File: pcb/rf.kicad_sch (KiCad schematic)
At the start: 0 parts

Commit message: tons of work on rf and mcu
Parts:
- added C41, C51: 22uF, symbol Device:C_Small
- added C42: 4.7uF, symbol Device:C_Small
- added C43, C44: 100nF, symbol Device:C_Small
- added C45: 1uF, symbol Device:C_Small
- added C46, C47: 1uF, symbol Device:C
- added C48, C49: 2.2uF, symbol Device:C
- added C50: 1nF, symbol Device:C
- added C52, C53, C54, C55, C56, C57, C58, C59, C60, C61, C62, C63, C64, C65, C66, C67: C, symbol Device:C
- added D2, D3: D_TVS, symbol Device:D_TVS
- added FB3, FB4, FB5: FerriteBead_Small, symbol Device:FerriteBead_Small
- added J4, J5: Conn_Coaxial, symbol Connector:Conn_Coaxial
- added L10, L11, L12, L13, L14, L3, L4, L5, L6, L7, L8, L9: L, symbol Device:L
- added L2: 2.2uH, symbol Device:L
- added TP1: GPS_D-, symbol Connector:TestPoint
- added TP2: GPS_D+, symbol Connector:TestPoint
- added U4: ~, symbol lr2021_new:lr2021
- added U5: NEO-M9N, RF_GPS:ublox_NEO, symbol RF_GPS:NEO-M9N
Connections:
- new net: C58.1, C59.1, L8.2
- new net: C57.1, C59.2, D2.2 (A2), J4.1 (In), L6.2, L7.1
- new net: C61.1, C62.1, L10.2
- new net: C53.1, L4.2
- new net: C53.2, C54.1, C55.1, L5.1
- new net: FB5.2, U4.13 (VPAX1)
- new net: C63.1, L11.2
- new net: C65.2, C66.1, L12.2, L13.1
- new net: C62.2, C67.1, D3.2 (A2), J5.1 (In), L13.2, L14.1
- new net: C55.2, C56.1, L5.2, L6.1
- new net: FB4.2, U4.12 (VDCC1)
- new net: L2.2, U4.14 (LXB)
- new net: L2.1, U4.16 (LXA)
- new net: U5.10 (GND), U5.12 (GND), U5.13 (GND), U5.24 (GND)
- new net: TP1.1, U5.5 (USB_DM)
- new net: TP2.1, U5.6 (USB_DP)
- new net: C63.2, C64.1, C65.1, L12.1
- new net +3.3V: FB3.1
- new net GND: C41.2, C42.2, C43.2, C44.2, C45.2, C46.2, C47.2, C48.2, C49.2, C50.2, C51.2, C52.1, C54.2, C56.2, C57.2, C58.2, C60.1, C61.2, C64.2, C66.2, C67.2, D2.1 (A1), D3.1 (A1), J4.2 (Ext), J5.2 (Ext), L14.2, L7.2, U4.0 (GND), U4.15 (GND_DCC), U4.30 (GND)
- new net hfi: L10.1, U4.31 (RFI_HF)
- new net hfo: L11.1, L9.2, U4.32 (RFO_HF)
- new net lfi: L8.1, U4.29 (RFI_LF)
- new net lfo: L3.2, L4.1, U4.27 (RFO_LF2), U4.28 (RFO_LF1)
- new net lr2021_vbat: C41.1, C42.1, C43.1, C44.1, C45.1, C51.1, FB3.2, U4.17 (VBAT)
- new net lr2021_vdcc: C46.1, C47.1, FB4.1, U4.26 (VDCC2)
- new net lr2021_vpax: C48.1, C49.1, FB5.1, U4.2 (VPAX2)
- new net lr_busy: U4.25 (BUSY)
- new net lr_irq1: U4.7 (DIO11)
- new net lr_irq2: U4.8 (DIO10)
- new net lr_miso: U4.21 (MISO)
- new net lr_mosi: U4.22 (MOSI)
- new net lr_nrst: U4.20 (NRST)
- new net lr_nss: U4.24 (NSS)
- new net lr_sck: U4.23 (SCK)
- new net vr_pa: C50.1, C52.2, C60.2, L3.1, L9.1, U4.1 (VR_PA)
- no-connect marks 0 -> 6
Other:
- note added: "semi insane vcc decoupling"
- note added: "vdcc decoupling"
- note added: "vpax decoupling"

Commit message: added missing files, rf stuff done I think (hope)
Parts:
- added AE1: Antenna, symbol Device:Antenna
- added C68: 100nF, symbol Device:C_Small
- added C69, C70: 22uF, symbol Device:C_Small
- added C71: 1uF, symbol Device:C
- added D4: D_TVS, symbol Device:D_TVS
- added JP1: NC, symbol Jumper:SolderJumper_2_Bridged
- added L15: 9.1nH, symbol Device:L
- added TP3: GPS_SDA, symbol Connector:TestPoint
- added TP4: GPS_SCL, symbol Connector:TestPoint
- added TP5: GPS_BOOT, symbol Connector:TestPoint
- added U6: ~, symbol alnd-wb-0013-t:ALND-WB-0013-T
- added Y3: ECS-TXO-32CSMV-320-AN-TR, ECSTXO32CSMV320ANTR, symbol ECS-TXO-32CSMV-320-AN-TR:ECS-TXO-32CSMV-320-AN-TR
- C52, C60: value C -> 47pF
- C53: value C -> 22pF
- C54: value C -> 7.5pF
- C55, C57: value C -> 1.8pF
- C56: value C -> 3.9pF
- C58: value C -> 2.2pF
- C59, C62: value C -> 18pF
- C61: value C -> idk; now not fitted
- C63: value C -> 6.8pF
- C64: value C -> 2.7pF
- C65: value C -> 1.1pF
- C66: value C -> 1.2pF
- C67: value C -> 2.0pF
- L10: value L -> 2.4nH
- L11: value L -> 1.5nH
- L12: value L -> 1.6nH
- L13: value L -> 1.1nH
- L14: value L -> idk; now not fitted
- L3: value L -> 12nH
- L4: value L -> 4.7nH
- L5: value L -> 3.9nH
- L6: value L -> 7.5nH
- L7: value L -> 22nH
- L8: value L -> 24nH
- L9: value L -> 18nH
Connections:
- net +3.3V: now also U5.22 (V_BCKP), U5.23 (VCC), U5.7 (VDD_USB), C69.1, C70.1, JP1.1 (A)
- net GND: now also U5.10 (GND), U5.12 (GND), U5.13 (GND), U5.24 (GND), C68.1, C69.2, C70.2, C71.2, D4.1 (A1), U6.1 (GND), U6.2 (GND), Y3.1 (GROUND_1), Y3.2 (GROUND_2)
- net lr_xtalin: now reaches U4.4 (XTA)
- net lr_xtalin: now also Y3.3 (OUTPUT)
- net lr_vtcxo: now reaches U4.6 (VTXCO)
- net lr_vtcxo: now also C68.2, Y3.4 (VDD)
- net at U5.1 (~{SAFEBOOT}): now also TP5.1
- net at U5.11 (RF_IN): now also U6.6 (RFOUT)
- net at U5.18 (SDA/~{SPI_CS}): now also TP3.1
- net at U5.19 (SCL/SPI_CLK): now also TP4.1
- net at U5.2 (D_SEL): now also JP1.2 (B)
- net gps_rx: now reaches U5.20 (TXD/SPI_MISO)
- net gps_tx: now reaches U5.21 (RXD/SPI_MOSI)
- net gps_pps: now reaches U5.3 (TIMEPULSE)
- net gps_rst: now reaches U5.8 (~{RESET})
- net at U5.9 (VCC_RF): now also C71.1, U6.4 (VDD), U6.5 (Ven)
- new net: AE1.1 (A), D4.2 (A2), L15.2
- new net: L15.1, U6.3 (RFIN)
- no-connect marks 6 -> 9
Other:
- note added: "32mhz tcxo"
- note added: "gps"
- note added: "high frequency matching"
- note added: "lora module"
- note added: "low frequency matching"
- moved on the sheet: C41, C42, C43, C44, C45, C46, C47, C48, C49, C50, C51, C52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

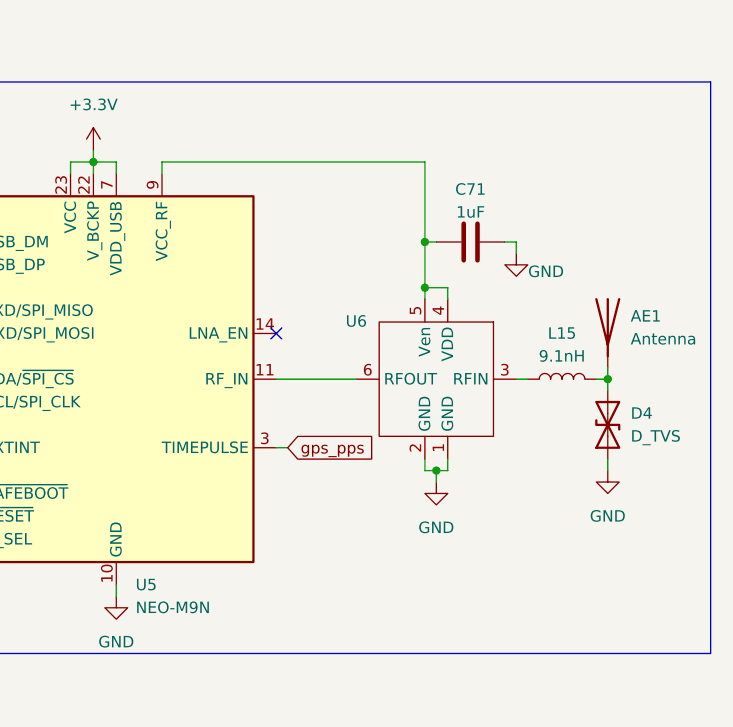
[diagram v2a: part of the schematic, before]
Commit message: sensors pretty much done (still need to add high g_
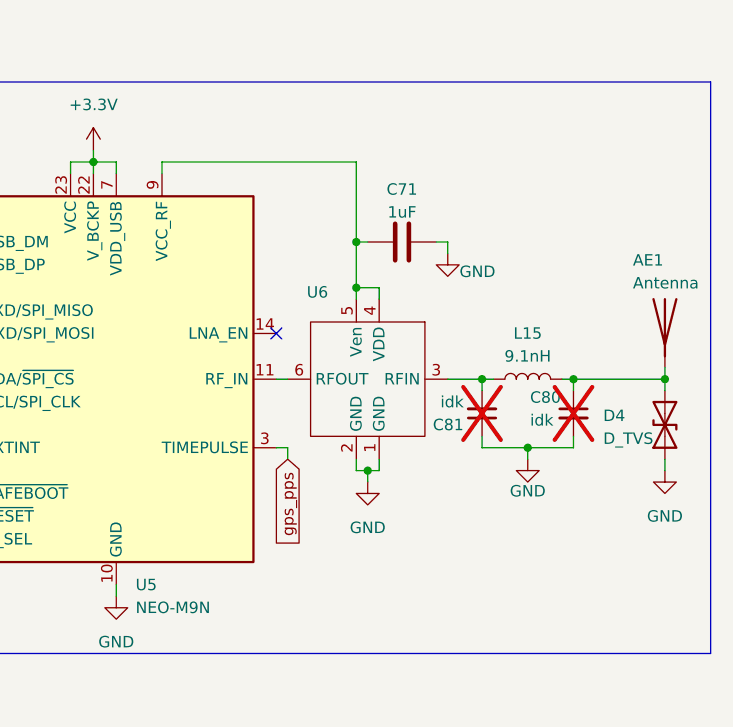
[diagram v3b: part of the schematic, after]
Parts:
- added C80, C81: idk, symbol Device:C_Small
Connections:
- net GND: now also C80.2, C81.1
- net at AE1.1 (A), D4.2 (A2), L15.2: now also C80.1
- net at L15.1, U6.3 (RFIN): now also C81.2
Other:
- moved on the sheet: AE1, C71, D4, L15, U6

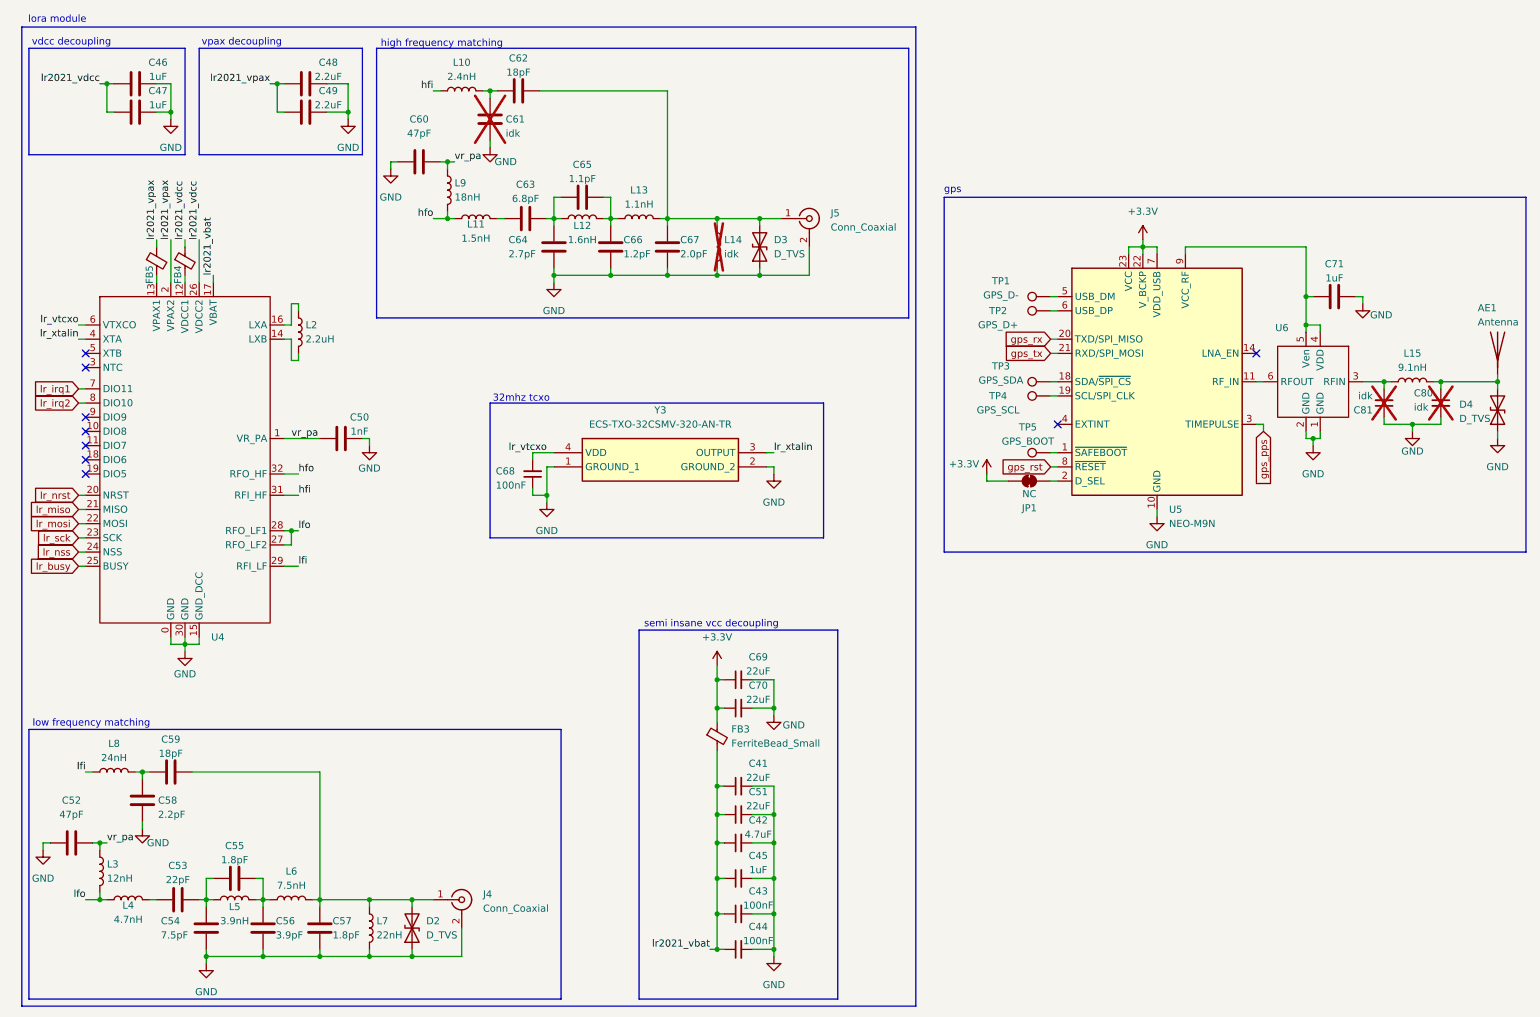
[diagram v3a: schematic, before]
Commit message: got fets figured out (finally), can integrated, a 5v regulator, sensors added - overall great progress!
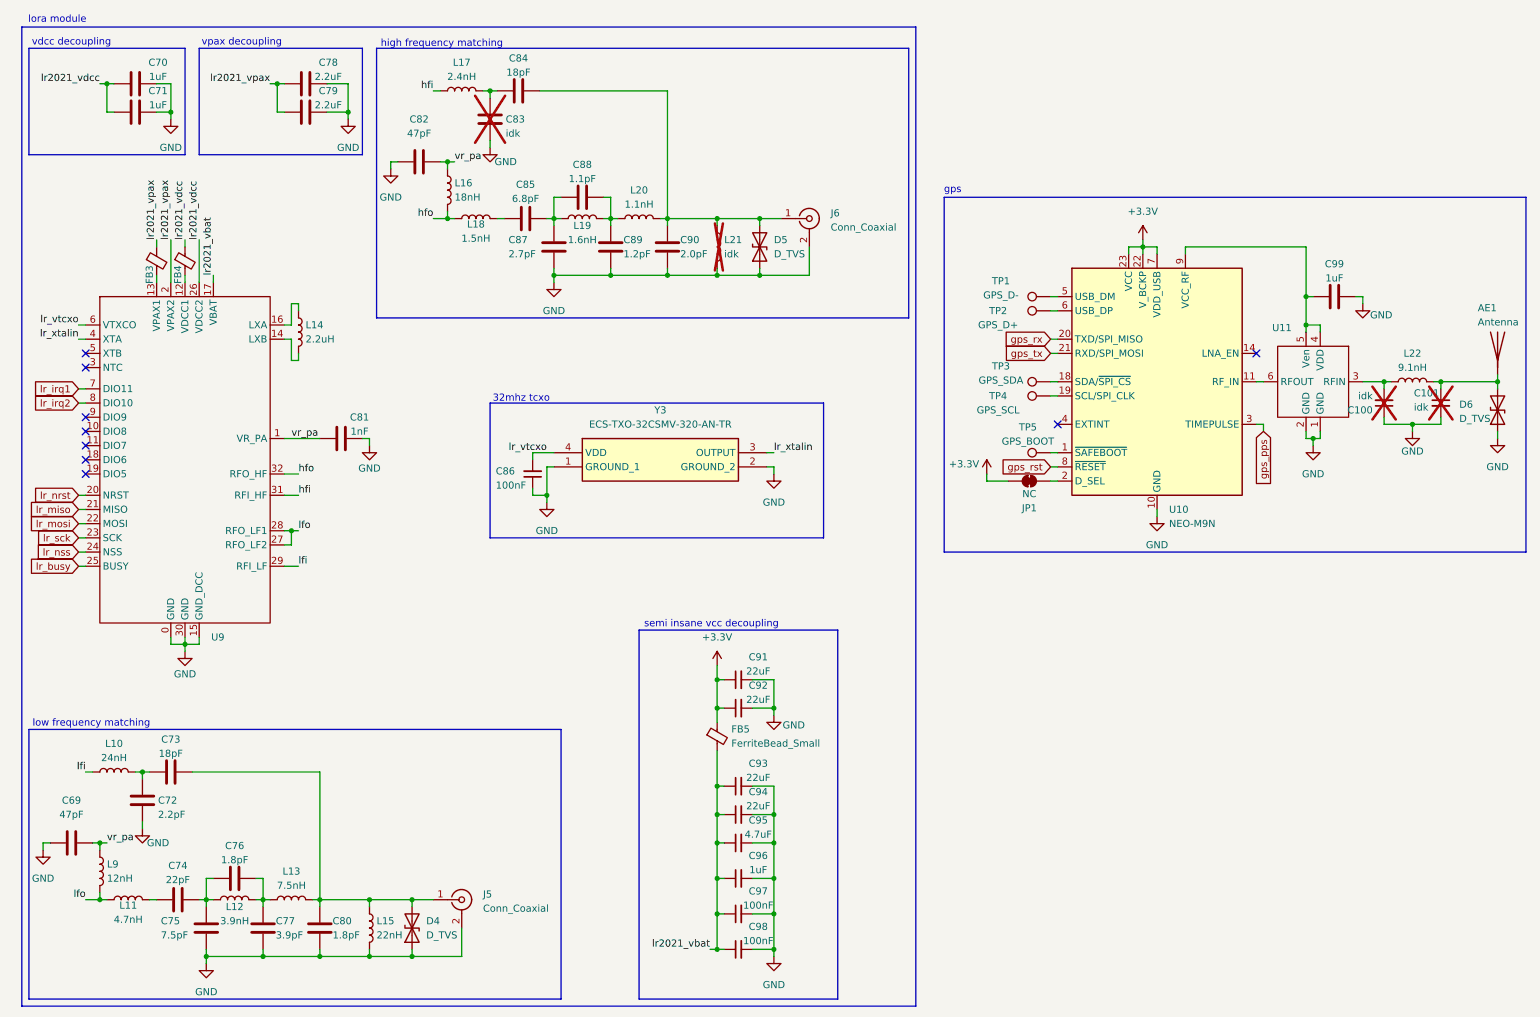
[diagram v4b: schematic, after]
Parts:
- renumbered C81 to C100, C80 to C101, C52 to C69, C46 to C70, C47 to C71, C58 to C72, C59 to C73, C53 to C74, C54 to C75, C55 to C76, C56 to C77, C48 to C78, C49 to C79, C57 to C80, C50 to C81, C60 to C82, C61 to C83, C62 to C84, C63 to C85, C68 to C86, C64 to C87, C65 to C88, C66 to C89, C67 to C90, C69 to C91, C70 to C92, C41 to C93, C51 to C94, C42 to C95, C45 to C96, C43 to C97, C44 to C98, C71 to C99, D2 to D4, D3 to D5, D4 to D6, FB5 to FB3, FB3 to FB5, J4 to J5, J5 to J6, L8 to L10, L4 to L11, L5 to L12, L6 to L13, L2 to L14, L7 to L15, L9 to L16, L10 to L17, L11 to L18, L12 to L19, L13 to L20, L14 to L21, L15 to L22, L3 to L9, U5 to U10, U6 to U11, U4 to U9

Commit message: pretty much everything on schem done, though need to add circuit protection stuff and break out remaining pins
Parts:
- AE1: value Antenna -> AANI-PP-0055
- C102: renamed from C100; value idk -> dnp
- C103: renamed from C101; value idk -> dnp
- C85: renamed from C83; value idk -> dnp
- L15: renamed from L21; value idk -> dnp
- U11: value ~ -> lna
- U9: value ~ -> lr2021
- renumbered C98 to C100, C99 to C101, C69 to C71, C70 to C72, C71 to C73, C72 to C74, C73 to C75, C74 to C76, C75 to C77, C76 to C78, C77 to C79, C78 to C80, C79 to C81, C80 to C82, C81 to C83, C82 to C84, C84 to C86, C85 to C87, C86 to C88, C87 to C89, C88 to C90, C89 to C91, C90 to C92, C91 to C93, C92 to C94, C93 to C95, C94 to C96, C95 to C97, C96 to C98, C97 to C99, D4 to D7, D5 to D8, D6 to D9, J5 to J7, J6 to J8, JP1 to JP5, L16 to L10, L17 to L11, L18 to L12, L19 to L13, L20 to L14, L22 to L16, L9 to L3, L10 to L4, L11 to L5, L12 to L6, L13 to L7, L14 to L8, L15 to L9, Y3 to Y5
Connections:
- net gps_rx renamed gps_mrx
- net gps_tx renamed gps_mtx

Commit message: yay schematic pretty much good, though I'm going to have to redo some work to split it into multiple kicad projects so I can have multiple separate boards
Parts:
- AE1: footprint (none) -> AANI-PP-0055:AANI-PP-0055
- C100, C102, C103, C99: footprint (none) -> Capacitor_SMD:C_0402_1005Metric
- C101, C72, C73, C97, C98: footprint (none) -> Capacitor_SMD:C_0603_1608Metric
- C80, C81: footprint (none) -> Capacitor_SMD:C_0805_2012Metric
- C93, C94, C95, C96: footprint (none) -> Capacitor_SMD:C_1210_3225Metric
- L16: footprint (none) -> Inductor_SMD:L_0402_1005Metric
- U11: footprint (none) -> ALND-WB-0013-T:ALND-WB-0013-T
- Y5: footprint ECSTXO32CSMV320ANTR -> ECS-TXO-32CSMV-320-AN:ECSTXO32CSMV320ANTR
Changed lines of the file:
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@@
 			)
 		)
-		(property "Footprint" ""
+		(property "Footprint" "Capacitor_SMD:C_0805_2012Metric"
 			(at 68.58 29.5148 0)
 			(effects
@@
 			)
 		)
-		(property "Footprint" ""
+		(property "Footprint" "Capacitor_SMD:C_0603_1608Metric"
 			(at 38.1 34.5948 0)
 			(effects
@@
 			)
 		)
-		(property "Footprint" ""
+		(property "Footprint" "Capacitor_SMD:C_0402_1005Metric"
 			(at 257.81 87.63 0)
 			(effects
@@
 			)
 		)
-		(property "Footprint" ""
+		(property "Footprint" "AANI-PP-0055:AANI-PP-0055"
 			(at 278.13 77.47 0)
 			(effects
@@
 			)
 		)
-		(property "Footprint" "ECSTXO32CSMV320ANTR"
+		(property "Footprint" "ECS-TXO-32CSMV-320-AN:ECSTXO32CSMV320ANTR"
 			(at 143.51 191.44 0)
 			(effects
@@
 			)
 		)
-		(property "Footprint" ""
+		(property "Footprint" "Capacitor_SMD:C_0603_1608Metric"
 			(at 142.24 172.72 0)
 			(effects
@@
 			)
 		)
-		(property "Footprint" ""
+		(property "Footprint" "Capacitor_SMD:C_1210_3225Metric"
 			(at 142.24 156.21 0)
 			(effects
@@
 			)
 		)
-		(property "Footprint" ""
+		(property "Footprint" "Capacitor_SMD:C_1210_3225Metric"
 			(at 142.24 142.24 0)
 			(effects
@@
 			)
 		)
-		(property "Footprint" ""
+		(property "Footprint" "Capacitor_SMD:C_0805_2012Metric"
 			(at 68.58 34.5948 0)
 			(effects
@@
 			)
 		)
-		(property "Footprint" ""
+		(property "Footprint" "Capacitor_SMD:C_0603_1608Metric"
 			(at 142.24 166.37 0)
 			(effects
@@
 			)
 		)
-		(property "Footprint" ""
+		(property "Footprint" "Capacitor_SMD:C_0603_1608Metric"
 			(at 252.73 67.6148 0)
 			(effects
@@
 			)
 		)
-		(property "Footprint" ""
+		(property "Footprint" "Capacitor_SMD:C_0402_1005Metric"
 			(at 267.97 87.63 0)
 			(effects
@@
 			)
 		)
-		(property "Footprint" ""
+		(property "Footprint" "ALND-WB-0013-T:ALND-WB-0013-T"
 			(at 236.22 77.47 0)
 			(effects
@@
 			)
 		)
-		(property "Footprint" ""
+		(property "Footprint" "Inductor_SMD:L_0402_1005Metric"
 			(at 262.89 83.82 0)
 			(effects
@@
 			)
 		)
-		(property "Footprint" ""
+		(property "Footprint" "Capacitor_SMD:C_0603_1608Metric"
 			(at 38.1 29.5148 0)
 			(effects
@@
 			)
 		)
-		(property "Footprint" ""
+		(property "Footprint" "Capacitor_SMD:C_1210_3225Metric"
 			(at 142.24 137.16 0)
 			(effects
@@
 			)
 		)
-		(property "Footprint" ""
+		(property "Footprint" "Capacitor_SMD:C_0402_1005Metric"
 			(at 142.24 179.07 0)
 			(effects
@@
 			)
 		)
-		(property "Footprint" ""
+		(property "Footprint" "Capacitor_SMD:C_1210_3225Metric"
 			(at 142.24 161.29 0)
 			(effects
@@
 			)
 		)
-		(property "Footprint" ""
+		(property "Footprint" "Capacitor_SMD:C_0402_1005Metric"
 			(at 142.24 185.42 0)
 			(effects
